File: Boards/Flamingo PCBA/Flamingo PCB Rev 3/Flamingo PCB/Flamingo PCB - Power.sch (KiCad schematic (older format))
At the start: 15 parts

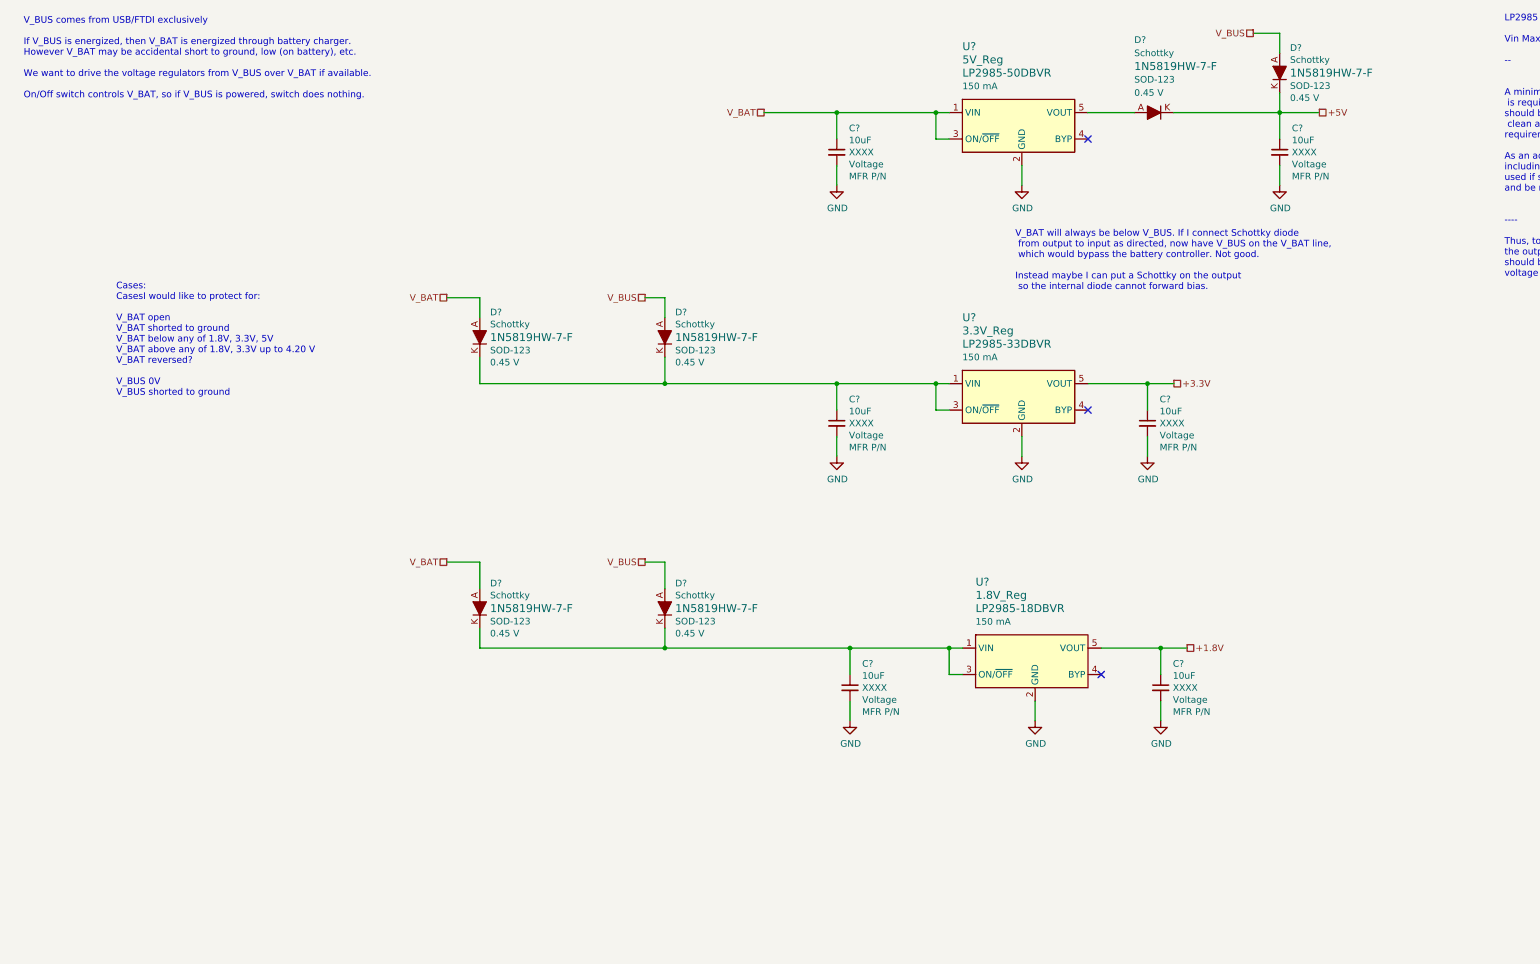
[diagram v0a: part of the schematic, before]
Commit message: NOSTUFF 5V LDO bc not needed. Added Sch diode on 5v LDO.
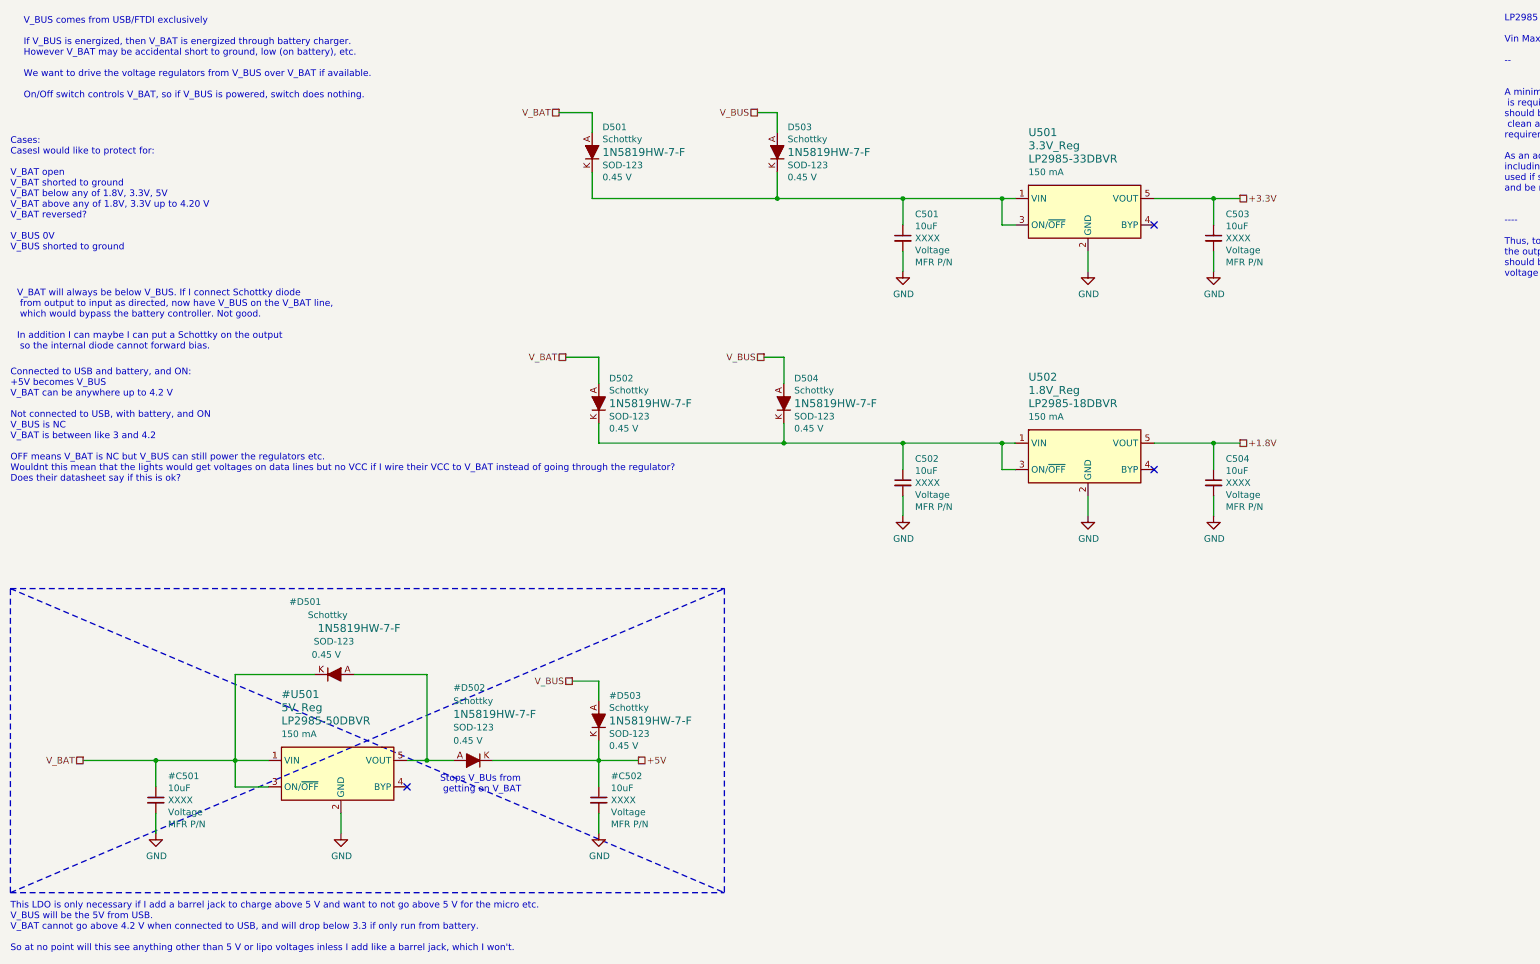
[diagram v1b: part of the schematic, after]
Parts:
- removed C? (x2): 10uF, symbol MyCapacitors:C_Small_vert
- removed D? (x2): Schottky, digikey-footprints:SOD-123, symbol dk_Diodes-Rectifiers-Single:1N5819HW-7-F
- removed U?: 5V_Reg, digikey-footprints:SOT-753, symbol MyICs:3.3V_Reg
- gave numbers to parts that had none: 10
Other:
- note added: "Connected to USB and battery, and ON: \n+5V becomes V_BUS\nV_BAT can be anywhere up to 4.2 V\n\nNot connected to USB, with battery, and ON\nV_BUS is NC\nV_BAT is between like 3 and 4.2\n\nOFF means V_BAT is NC but V_BUS can still power the regulators etc.\nWouldnt this mean that the lights would get voltages on data lines but no VCC if I wire their VCC to V_BAT instead of going through the regula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"
- note added: "Stops V_BUs from\n getting on V_BAT"
- note added: "This LDO is only necessary if I add a barrel jack to charge above 5 V and want to not go above 5 V for the micro etc. \nV_BUS will be the 5V from USB.\nV_BAT cannot go above 4.2 V when connected to USB, and will drop below 3.3 if only run from battery. \n\nSo at no point will this see anything other than 5 V or lipo voltages inless I add like a barrel jack, which I won't."
- note added: "V_BAT will always be below V_BUS. If I connect Schottky diode\n from output to input as directed, now have V_BUS on the V_BAT line,\n which would bypass the battery controller. Not good.\n\nIn addition I can maybe I can put a Schottky on the output\n so the internal diode cannot forward bias."
- note removed: "V_BAT will always be below V_BUS. If I connect Schottky diode\n from output to input as directed, now have V_BUS on the V_BAT line,\n which would bypass the battery controller. Not good.\n\nInstead maybe I can put a Schottky on the output\n so the internal diode cannot forward bias."
- moved on the sheet: C501, C502, C503, C504, D501, D502, D503, D504, U501, U502

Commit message: Moved Battery Charger sheet into Power sheet
Right before addition of power sharing mosfet, maybe
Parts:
- added C? (x2): 10uF, Capacitors_SMD:C_0805_HandSoldering, symbol MyCapacitors:CP1_Small_vert
- added D?: Red/Charging, LEDs:LED_0603_HandSoldering, symbol MyLEDs:LED_ALT_vert
- added D?: Green/Done, LEDs:LED_0603_HandSoldering, symbol MyLEDs:LED_ALT_vert
- added J?: Wire Switch Here, digikey-footprints:PinHeader_1x2_P2mm_Drill1mm_RA, symbol dk_Rectangular-Connectors-Headers-Male-Pins:S2B-PH-K-S_LF__SN_
- added J?: JST PH Battery Connector, digikey-footprints:PinHeader_1x2_P2mm_Drill1mm_RA, symbol dk_Rectangular-Connectors-Headers-Male-Pins:S2B-PH-K-S_LF__SN_
- added J?: 10103594-0001LF, digikey-footprints:USB_Micro_B_Female_10103594-0001LF, symbol dk_USB-DVI-HDMI-Connectors:10103594-0001LF
- added JP?: Solder Jumper, Jumper:SolderJumper-2_P1.3mm_Open_Pad1.0x1.5mm, symbol Jumper:SolderJumper_2_Open
- added R? (x2): 1.5k, Resistors_SMD:R_0603_HandSoldering, symbol MyResistors:R_vert
- added R?: 2.49k, Resistors_SMD:R_0603_HandSoldering, symbol MyResistors:R_vert
- added R?: 10k, Resistors_SMD:R_0603_HandSoldering, symbol MyResistors:R_vert
- added U?: MCP73831T-2ATI_OT, digikey-footprints:SOT-753, symbol MyICs:MCP73831T-2ATI_OT
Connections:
- net V_BUS is gone; now on net GND: D503.A, D504.A
- net GND: now also C?.1, C?.2, C?.2, D?.1 (K), D?.2 (A), J?.1, J?.2, J?.5, J?.SH, R?.2, R?.2, U?.2 (VSS), U?.4 (VDD)
- net V_BAT: now also J?.1
- new net: D?.1 (K), R?.1
- new net: R?.1, R?.2, U?.1 (STAT)
- new net: D?.2 (A), R?.2
- new net: JP?.2 (B), R?.1
- new net: JP?.1 (A), R?.1, U?.5 (PROG)
- new net: C?.1, J?.1, J?.2, U?.3 (VBAT)
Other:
- note added: "--------FLOW CHART--------\n\n###SHUTDOWN MODE\nVDD < VUVLO\nVDD < VBAT\nor\nPROG > 200 k\nSTAT = High Z\n\n###PRECONDITIONING \nCharge Current = IPREG\nSTAT = LOW\n\n###FAST CHARGE \nAlso get here if VBAT > VPTH from SHUTDOWN \nor \nVBAT < VRTH from CHARGE COMPLETE\n\nCharge Current = IREG\nSTAT = LOW\n\n###CONSTANT VOLTAGE \nCharge Voltage = VREG\nSTAT = LOW\n\n###CHARGE MODE \nSTAT = HIGH (MCP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"
- note added: "1) Run off USB while charging: Battery may not charge since load is on V_BAT, and all current goes through battery charger."
- note added: "10118194-0001LF would have been nicer, \nas it says 4 DIP legs, vis this SMT plus 2 DIP,\nbut was shipping like 3 months out when I made this"
- note added: "A search for 0603 OSRAM leds\n\nhttps://www.digikey.com/short/zwdccj\nBlue\nGreen\norange\nRed\nWhite\nWhite Cool\nYellow"
- note added: "HIGH when charging is done"
- note added: "Open: 10k = 100 mA\nClosed: 2.0k = 500 mA\n\nBatt charging rate:\n\n10k = 100mA *\n5.0k = 200 mA\n2.0k = 500 mA *\n1.0k = 1000mA \n\nAdafruit typically does 0.5C for their batteries\n2500 mAh capacity - 1200 mA charge current"
- note added: "TODO:\nCHECK POLARITY"
- note added: "TODO:\nNEED TO FIND A GOOD SOCKET FOR THE SWITCH CABLE\nMIGHT JUST NOT POPULATE AND SOLDER DIRECT"
- note added: "USE CASES\n\n[BATT CONNECTED] [SWITCH POSITION] [USB CONNECTED]\n\n1) I want to charge the device from USB, it is off, batt connected [Batt present] [OFF] [USB present]\n\n2) I want to charge the device from USB, it is on, batt connected [Batt present] [ON] [USB present]\n\n3) has no batt, is connected to USB, it is off. [No batt] [OFF] [USB present]\n\n4) Has no batt, is connected to USB, it is 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"
- note added: "V_BUS comes from USB\n\nOn/Off switch controls V_BAT"
- note added: "Vf = 1.8V, 2 mA Ityp\n5V-1.8 = 3.2V\n3.2V/1.5k = 2.1 mA"
- note added: "Will need to take some approach to negotiating higher power delivery\n if I am planning on using more than 500 mA. For example, \na 2000 mAh LiPo charges at 1200 mA.\n\nApproaches are:\n\nDont.\nhttps://www.maximintegrated.com/en/design/technical-documents/tutorials/4/4803.html#3"
- note added: "battery"
- note added: "https://easyeda.com/gerdmuller.de/lithium-battery-charger-mcp73831-with-load-sharing"
- note added: "https://www.eevblog.com/forum/microcontrollers/rechargeable-battery-solution-for-mcu-projects/msg630455/#msg630455"
- note added: "independent of the capacitor’s minimum\nEffective Series Resistance (ESR) value. The actual\nvalue of the capacitor (and its associated ESR)\ndepends on the output load current. A 4.7 µF ceramic,\ntantalum or aluminum electrolytic capacitor at the\noutput is usually sufficient to ensure stability for output\ncurrents up to a 500 mA."
- moved on the sheet: C501, C502, C503, C504, D501, D502, D503, D504, U501, U502
